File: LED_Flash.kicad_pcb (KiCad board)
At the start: 2 copper layers, 20.5 x 33 mm, 13 parts, among them P1 P_In, P3 Trig_In, Q1 Q_NMOS_SGD

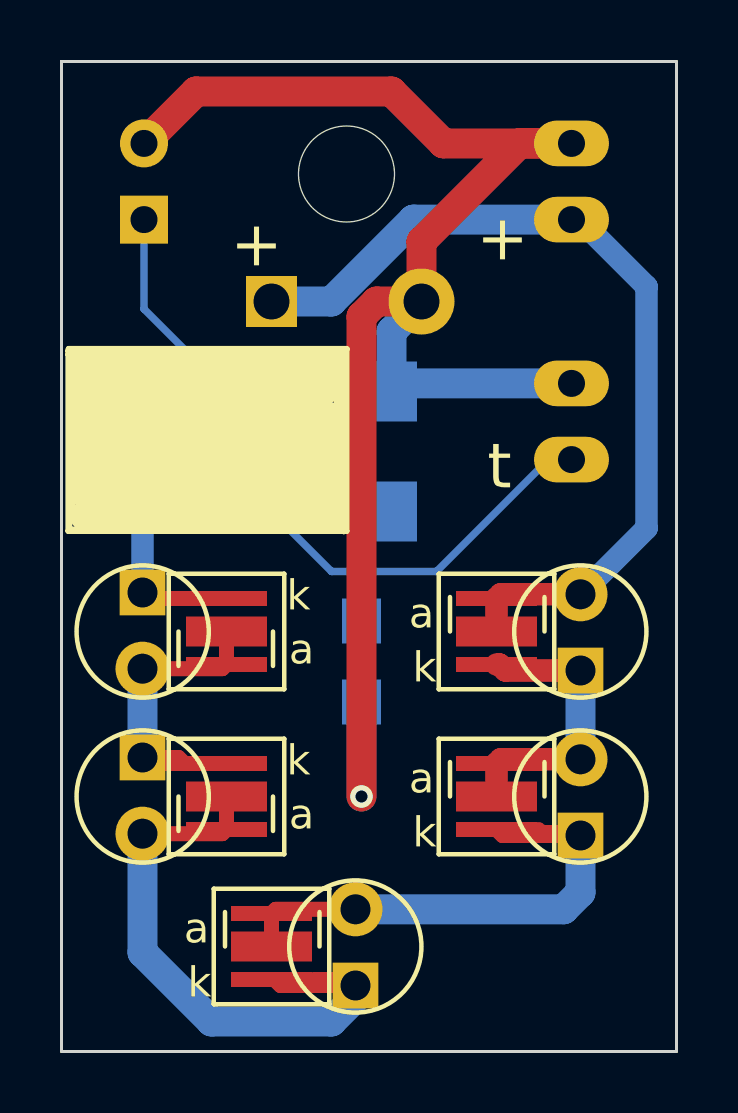
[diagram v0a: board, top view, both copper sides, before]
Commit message: Add some examples to schematic and part numbers
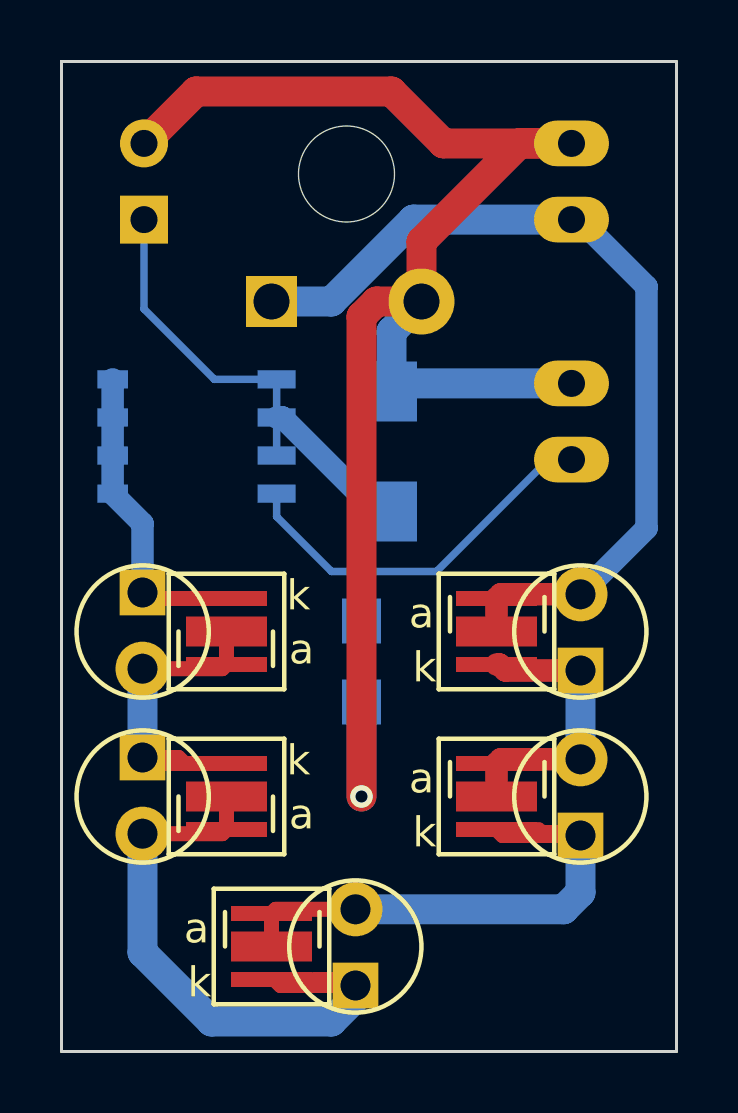
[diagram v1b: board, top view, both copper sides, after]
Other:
- board text removed: "+"
- board text removed: "t"
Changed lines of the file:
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@@
     (area 60.442857 63.39381 87.142858 101.050001)
     (thickness 1.6)
-    (drawings 50)
+    (drawings 14)
     (tracks 95)
     (zones 0)
@@
   (page A4)
   (layers
-    (0 F.Cu signal hide)
-    (31 B.Cu signal hide)
-    (32 B.Adhes user hide)
-    (33 F.Adhes user hide)
-    (34 B.Paste user hide)
-    (35 F.Paste user hide)
-    (36 B.SilkS user hide)
+    (0 F.Cu signal)
+    (31 B.Cu signal)
+    (32 B.Adhes user)
+    (33 F.Adhes user)
+    (34 B.Paste user)
+    (35 F.Paste user)
+    (36 B.SilkS user)
     (37 F.SilkS user)
-    (38 B.Mask user hide)
-    (39 F.Mask user hide)
-    (40 Dwgs.User user hide)
-    (41 Cmts.User user hide)
-    (42 Eco1.User user hide)
+    (38 B.Mask user)
+    (39 F.Mask user)
+    (40 Dwgs.User user)
+    (41 Cmts.User user)
+    (42 Eco1.User user)
     (43 Eco2.User user)
     (44 Edge.Cuts user)
     (45 Margin user)
-    (46 B.CrtYd user hide)
+    (46 B.CrtYd user)
     (47 F.CrtYd user)
-    (48 B.Fab user hide)
-    (49 F.Fab user hide)
+    (48 B.Fab user)
+    (49 F.Fab user)
   )
   (setup
-    (last_trace_width 0.6)
+    (last_trace_width 1)
     (user_trace_width 0.5)
     (user_trace_width 0.75)
@@
     (mod_text_size 1 1)
     (mod_text_width 0.15)
-    (pad_size 1.78 0.61)
-    (pad_drill 0)
+    (pad_size 2.2 2.2)
+    (pad_drill 1.2)
     (pad_to_mask_clearance 0)
     (aux_axis_origin 0 0)
-    (visible_elements 7FFFFFFF)
+    (visible_elements FFFFFF7F)
     (pcbplotparams
       (layerselection 0x010f0_80000001)
@@
     (pad 2 smd rect (at -2.67 -1.905 180) (size 1.27 0.61) (layers B.Cu B.Paste B.Mask)
       (net 7 /Trig))
-    (pad 3 smd rect (at 2.5 -1.905 180) (size 1.78 0.61) (layers B.Cu B.Paste B.Mask)
+    (pad 3 smd rect (at 2.795 -1.905 180) (size 1.02 0.61) (layers B.Cu B.Paste B.Mask)
       (net 9 "Net-(D5-Pad1)"))
     (pad 3 smd rect (at 2.795 -0.635 180) (size 1.02 0.61) (layers B.Cu B.Paste B.Mask)
@@
     (pad 3 smd rect (at 2.795 0.635 180) (size 1.02 0.61) (layers B.Cu B.Paste B.Mask)
       (net 9 "Net-(D5-Pad1)"))
-    (pad 3 smd rect (at 2.495 1.905 180) (size 1.78 0.61) (layers B.Cu B.Paste B.Mask)
+    (pad 3 smd rect (at 2.795 1.905 180) (size 1.02 0.61) (layers B.Cu B.Paste B.Mask)
       (net 9 "Net-(D5-Pad1)"))
   )
@@
     (pad 1 np_thru_hole circle (at 0 0) (size 3.2 3.2) (drill 3.2) (layers *.Cu *.Mask F.SilkS))
   )
-  (gr_line (start 61.24 77.58) (end 61.24 77.63) (angle 90) (layer F.SilkS) (width 0.2))
-  (gr_line (start 70.51 77.58) (end 61.24 77.58) (angle 90) (layer F.SilkS) (width 0.2))
-  (gr_line (start 61.23 77.65) (end 61.25 77.65) (angle 90) (layer F.SilkS) (width 0.2))
-  (gr_line (start 61.23 83.65) (end 61.23 77.65) (angle 90) (layer F.SilkS) (width 0.2))
-  (gr_line (start 70.5 83.65) (end 61.23 83.65) (angle 90) (layer F.SilkS) (width 0.2))
-  (gr_line (start 70.5 77.6) (end 70.5 83.65) (angle 90) (layer F.SilkS) (width 0.2))
-  (gr_line (start 70.18 79.8) (end 70.1 79.8) (angle 90) (layer F.SilkS) (width 0.2))
-  (gr_line (start 70.18 78.94) (end 70.18 79.8) (angle 90) (layer F.SilkS) (width 0.2))
-  (gr_line (start 61.45 79.32) (end 61.83 79.32) (angle 90) (layer F.SilkS) (width 0.2))
-  (gr_line (start 61.45 82.19) (end 61.45 79.32) (angle 90) (layer F.SilkS) (width 0.2))
-  (gr_line (start 61.45 77.77) (end 61.45 82.19) (angle 90) (layer F.SilkS) (width 0.2))
-  (gr_line (start 70.36 77.77) (end 61.45 77.77) (angle 90) (layer F.SilkS) (width 0.2))
-  (gr_line (start 61.23 77.77) (end 70.36 77.77) (angle 90) (layer F.SilkS) (width 0.2))
-  (gr_line (start 61.26 77.65) (end 61.26 78.01) (angle 90) (layer F.SilkS) (width 0.2))
-  (gr_line (start 70.42 77.65) (end 61.26 77.65) (angle 90) (layer F.SilkS) (width 0.2))
-  (gr_line (start 70.41 83.66) (end 70.41 77.66) (angle 90) (layer F.SilkS) (width 0.2))
-  (gr_line (start 70.35 83.6) (end 70.41 83.66) (angle 90) (layer F.SilkS) (width 0.2))
-  (gr_line (start 61.65 83.6) (end 70.35 83.6) (angle 90) (layer F.SilkS) (width 0.2))
-  (gr_line (start 61.26 83.6) (end 61.65 83.6) (angle 90) (layer F.SilkS) (width 0.2))
-  (gr_line (start 61.26 83.31) (end 61.26 83.6) (angle 90) (layer F.SilkS) (width 0.2))
-  (gr_line (start 61.26 77.97) (end 61.26 83.31) (angle 90) (layer F.SilkS) (width 0.2))
-  (gr_line (start 61.37 77.97) (end 61.26 77.97) (angle 90) (layer F.SilkS) (width 0.2))
-  (gr_line (start 61.37 83.29) (end 61.37 77.97) (angle 90) (layer F.SilkS) (width 0.2))
-  (gr_line (start 70.3 83.29) (end 61.37 83.29) (angle 90) (layer F.SilkS) (width 0.2))
-  (gr_line (start 70.3 78.06) (end 70.3 83.29) (angle 90) (layer F.SilkS) (width 0.2))
-  (gr_line (start 61.78 83.15) (end 70 83.15) (angle 90) (layer F.SilkS) (width 1))
-  (gr_line (start 61.78 82.37) (end 70 82.37) (angle 90) (layer F.SilkS) (width 1))
-  (gr_line (start 61.78 81.5) (end 70 81.5) (angle 90) (layer F.SilkS) (width 1))
-  (gr_line (start 61.75 80.66) (end 69.97 80.66) (angle 90) (layer F.SilkS) (width 1))
-  (gr_line (start 61.72 79.85) (end 69.94 79.85) (angle 90) (layer F.SilkS) (width 1))
-  (gr_line (start 61.69 78.87) (end 69.91 78.87) (angle 90) (layer F.SilkS) (width 1))
-  (gr_line (start 61.66 78.09) (end 69.88 78.09) (angle 90) (layer F.SilkS) (width 1))
-  (gr_text t (at 75.6 81.5) (layer F.SilkS)
-    (effects (font (size 1.5 1.5) (thickness 0.3)))
-  )
-  (gr_text + (at 75.7 73.9) (layer F.SilkS)
-    (effects (font (size 1.5 1.5) (thickness 0.3)))
-  )
-  (gr_text + (at 67.5 74.1) (layer B.SilkS)
-    (effects (font (size 1.5 1.5) (thickness 0.3)) (justify mirror))
-  )
-  (gr_text + (at 67.5 74.1) (layer F.SilkS)
-    (effects (font (size 1.5 1.5) (thickness 0.3)))
-  )
   (gr_text - (at 73.5 77.5) (layer B.SilkS)

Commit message: Extra silk markings and change to SO-8 footprint
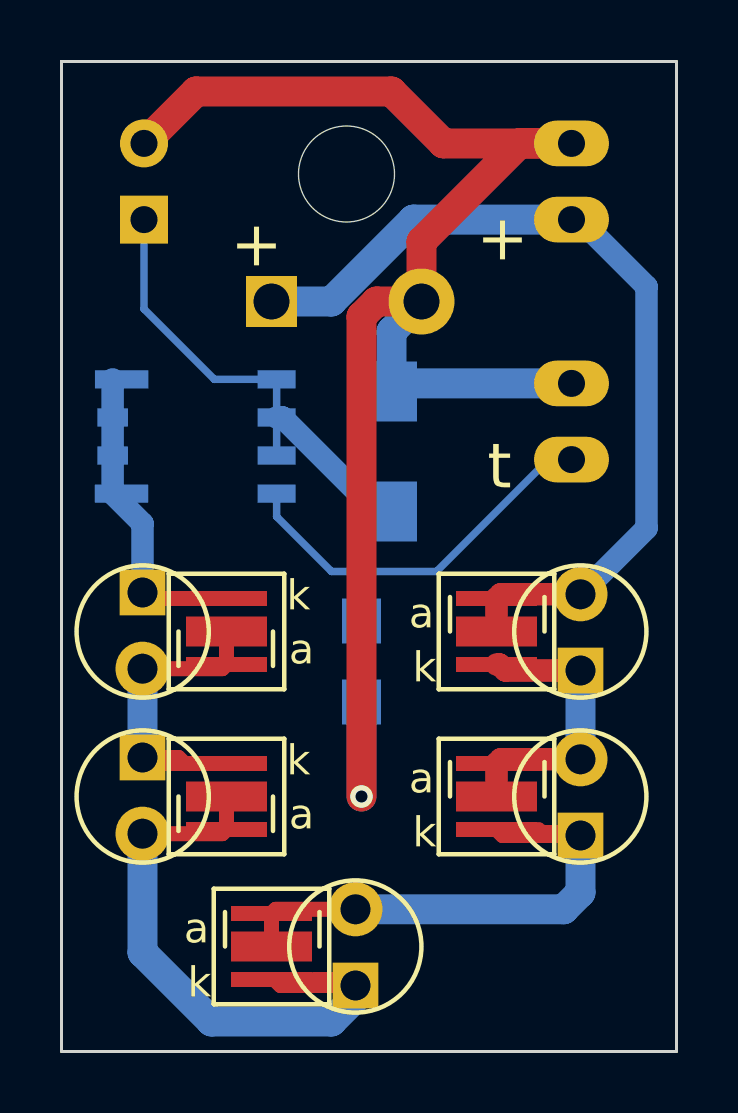
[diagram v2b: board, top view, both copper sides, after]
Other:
- board text added: "+"
- board text added: "t"
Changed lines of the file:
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@@
     (area 60.442857 63.39381 87.142858 101.050001)
     (thickness 1.6)
-    (drawings 14)
+    (drawings 18)
     (tracks 95)
     (zones 0)
@@
     (0 F.Cu signal)
     (31 B.Cu signal)
-    (32 B.Adhes user)
-    (33 F.Adhes user)
-    (34 B.Paste user)
-    (35 F.Paste user)
+    (32 B.Adhes user hide)
+    (33 F.Adhes user hide)
+    (34 B.Paste user hide)
+    (35 F.Paste user hide)
     (36 B.SilkS user)
     (37 F.SilkS user)
-    (38 B.Mask user)
-    (39 F.Mask user)
-    (40 Dwgs.User user)
-    (41 Cmts.User user)
-    (42 Eco1.User user)
+    (38 B.Mask user hide)
+    (39 F.Mask user hide)
+    (40 Dwgs.User user hide)
+    (41 Cmts.User user hide)
+    (42 Eco1.User user hide)
     (43 Eco2.User user)
     (44 Edge.Cuts user)
     (45 Margin user)
-    (46 B.CrtYd user)
+    (46 B.CrtYd user hide)
     (47 F.CrtYd user)
-    (48 B.Fab user)
-    (49 F.Fab user)
+    (48 B.Fab user hide)
+    (49 F.Fab user hide)
   )
   (setup
-    (last_trace_width 1)
+    (last_trace_width 0.6)
     (user_trace_width 0.5)
     (user_trace_width 0.75)
@@
     (mod_text_size 1 1)
     (mod_text_width 0.15)
-    (pad_size 2.2 2.2)
-    (pad_drill 1.2)
+    (pad_size 1.78 0.61)
+    (pad_drill 0)
     (pad_to_mask_clearance 0)
     (aux_axis_origin 0 0)
-    (visible_elements FFFFFF7F)
+    (visible_elements 7FFFFFFF)
     (pcbplotparams
       (layerselection 0x010f0_80000001)
@@
     (pad 2 smd rect (at -2.67 -1.905 180) (size 1.27 0.61) (layers B.Cu B.Paste B.Mask)
       (net 7 /Trig))
-    (pad 3 smd rect (at 2.795 -1.905 180) (size 1.02 0.61) (layers B.Cu B.Paste B.Mask)
+    (pad 3 smd rect (at 2.5 -1.905 180) (size 1.78 0.61) (layers B.Cu B.Paste B.Mask)
       (net 9 "Net-(D5-Pad1)"))
     (pad 3 smd rect (at 2.795 -0.635 180) (size 1.02 0.61) (layers B.Cu B.Paste B.Mask)
@@
     (pad 3 smd rect (at 2.795 0.635 180) (size 1.02 0.61) (layers B.Cu B.Paste B.Mask)
       (net 9 "Net-(D5-Pad1)"))
-    (pad 3 smd rect (at 2.795 1.905 180) (size 1.02 0.61) (layers B.Cu B.Paste B.Mask)
+    (pad 3 smd rect (at 2.495 1.905 180) (size 1.78 0.61) (layers B.Cu B.Paste B.Mask)
       (net 9 "Net-(D5-Pad1)"))
   )
@@
     (pad 1 np_thru_hole circle (at 0 0) (size 3.2 3.2) (drill 3.2) (layers *.Cu *.Mask F.SilkS))
   )
+  (gr_text t (at 75.6 81.5) (layer F.SilkS)
+    (effects (font (size 1.5 1.5) (thickness 0.3)))
+  )
+  (gr_text + (at 75.7 73.9) (layer F.SilkS)
+    (effects (font (size 1.5 1.5) (thickness 0.3)))
+  )
+  (gr_text + (at 67.5 74.1) (layer B.SilkS)
+    (effects (font (size 1.5 1.5) (thickness 0.3)) (justify mirror))
+  )
+  (gr_text + (at 67.5 74.1) (layer F.SilkS)
+    (effects (font (size 1.5 1.5) (thickness 0.3)))
+  )
   (gr_text - (at 73.5 77.5) (layer B.SilkS)
